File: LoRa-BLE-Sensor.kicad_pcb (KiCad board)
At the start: 4 copper layers, 96 x 80 mm, 123 parts, among them J1 SHF-105-01-X-D-SM, J2 Battery_Cell, J3 Conn_01x06_Socket, J4 Screw_Terminal_01x04, J5 Screw_Terminal_01x06, J6 Screw_Terminal_01x06, J7 Conn_01x10_Pin, J8 Conn_01x02_Socket, Q1 DMN67D7L, Q10 SQ2389ES, Q11 DMN62D0UDW-7, Q12 DMN62D0UDW-7, Q13 SQ2389ES, Q2 DMN67D7L, Q3 DMN67D7L, Q4 DMN67D7L, Q5 DMN67D7L, Q6 DMN67D7L, Q7 DMN67D7L, Q8 DMN67D7L, Q9 SQ2389ES, SW1 SW_Push, SW2 SW_Push, SW3 SW_Push, U1 RAK4630, U2 NPM1300-QEAA-R, U3 TLV61046ADBVR, U4 TLV61046ADBVR, U5 TLV61046ADBVR

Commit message: mounting holes + routing
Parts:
- added REF**: MountingHole_2.2mm_M2, MountingHole:MountingHole_2.2mm_M2, F.Cu at (67.5, 35.0)
- added REF**: MountingHole_2.2mm_M2, MountingHole:MountingHole_2.2mm_M2, F.Cu at (156.5, 35.0)
- added REF**: MountingHole_2.2mm_M2, MountingHole:MountingHole_2.2mm_M2, F.Cu at (67.5, 104.0)
- added REF**: MountingHole_2.2mm_M2, MountingHole:MountingHole_2.2mm_M2, F.Cu at (156.5, 104.0)
- moved D7 4.30 mm to (141.4, 59.8), turned to -90 degrees
- moved R8 0.55 mm to (130.3, 60.6)
- moved R11 0.06 mm to (127.8, 60.6)
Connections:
- Q3 pad 1: VOUT_SENSOR1 -> SENSOR1_PWR
- Q4 pad 1: VOUT_SENSOR1 -> SENSOR1_PWR
- Q7 pad 1: VOUT_SENSOR2 -> SENSOR2_PWR
- Q8 pad 1: VOUT_SENSOR2 -> SENSOR2_PWR
- R13 pad 1: VOUT_SENSOR2 -> SENSOR2_PWR
- R14 pad 1: VOUT_SENSOR2 -> SENSOR2_PWR
- R5 pad 1: VOUT_SENSOR1 -> SENSOR1_PWR
- R6 pad 1: VOUT_SENSOR1 -> SENSOR1_PWR
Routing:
- net VSYS: track 39.2 -> 140.7 mm, vias 11 -> 14
- net SENSOR2_IIN_NRF: track 2.31 -> 45.1 mm
- net SENSOR2_VIN_NRF: track 2.29 -> 41.5 mm
- net SENSOR2_PWR: track 33.7 -> 69.8 mm, vias 0 -> 4
- net SENSOR1_PWR: track 14.8 -> 50.2 mm, vias 0 -> 4
- net SENSOR3_D1_NRF: track 0.00 -> 34.4 mm
- net SENSOR3_D2_NRF: track 0.00 -> 33.3 mm
- net LDO2_OUT: track 45.2 -> 75.2 mm
- net VOUT_SENSOR1: track 24.9 -> 0.00 mm, vias 2 -> 0
- net BOOST2_FB_CTRL2: track 24.8 -> 43.9 mm
- net BOOST2_FB_CTRL1: track 25.7 -> 43.1 mm
- net VBOOST3: track 0.00 -> 17.0 mm
- net BOOST2_EN: track 27.3 -> 41.6 mm
- net SENSOR2_D1: track 1.70 -> 12.8 mm
- net SENSOR2_D2: track 1.70 -> 12.7 mm
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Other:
- board size 96 x 80 mm -> 96 x 79 mm

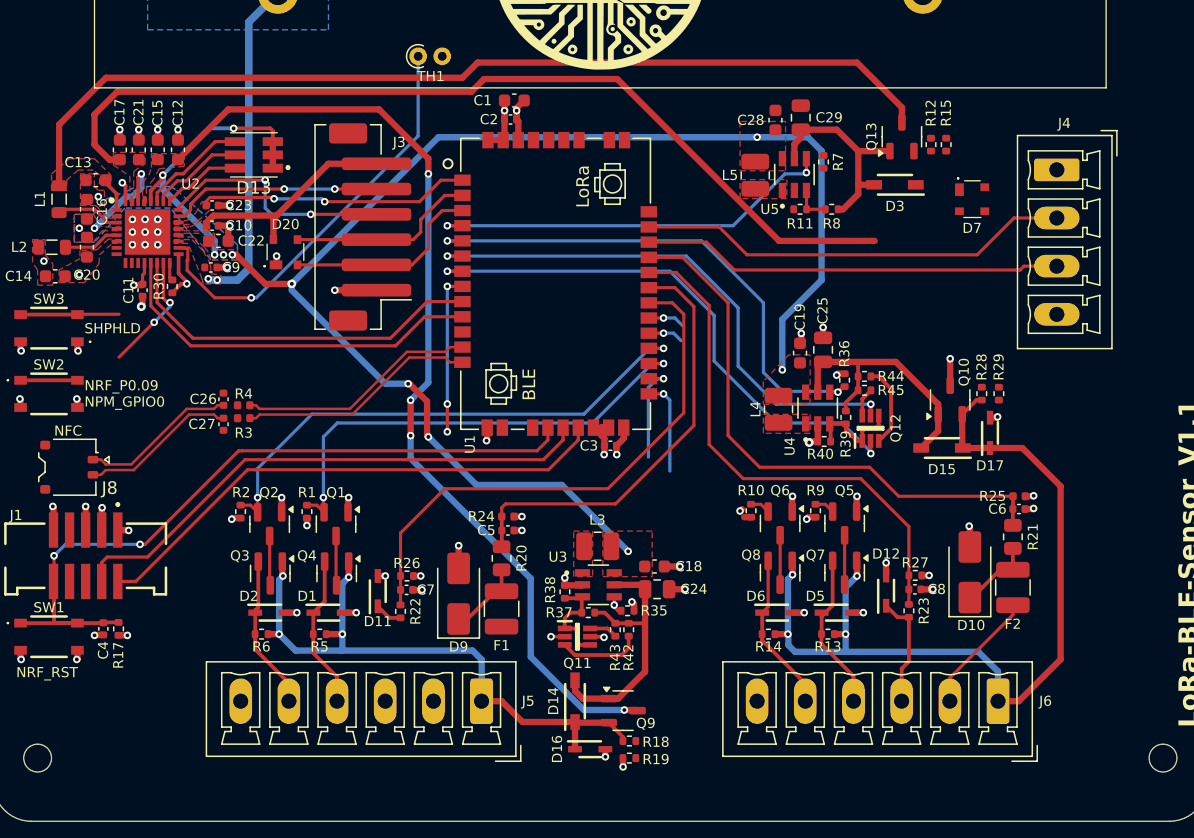
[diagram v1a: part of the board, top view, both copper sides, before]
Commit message: all tracks routed and DRC passed
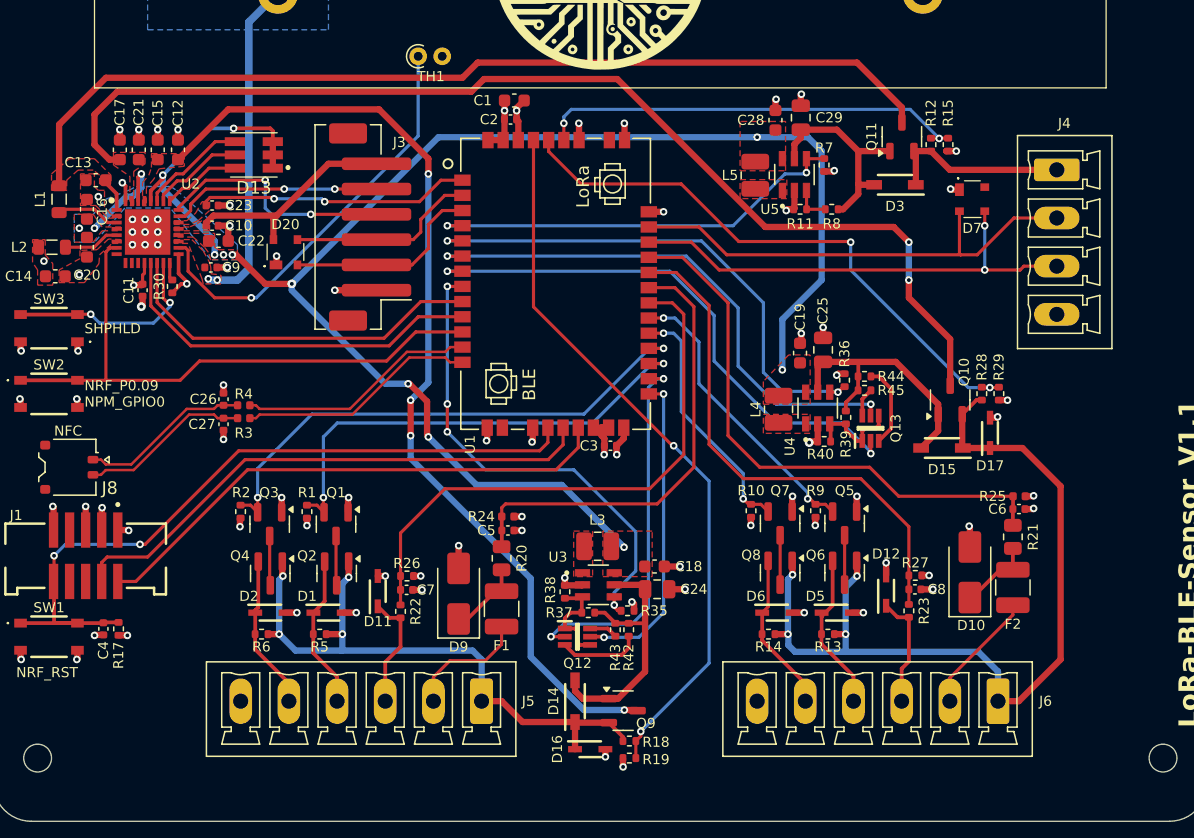
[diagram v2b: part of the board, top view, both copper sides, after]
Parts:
- moved R7 0.25 mm to (129.7, 57.1)
- moved R15 0.15 mm to (139.5, 55.5)
- renumbered Q13 to Q11, Q11 to Q12, Q12 to Q13, Q4 to Q2, Q2 to Q3, Q3 to Q4, Q7 to Q6, Q6 to Q7
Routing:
- net V_SENSOR1_READ: track 0.00 -> 57.1 mm, vias 0 -> 2
- net V_SENSOR2_READ: track 0.00 -> 46.2 mm, vias 0 -> 2
- net BUT1: track 4.50 -> 47.7 mm
- net V_SENSOR3_READ: track 0.00 -> 34.1 mm, vias 0 -> 2
- net BOOST1_EN: track 14.2 -> 38.8 mm
- net BOOST1_FB_CTRL2: track 9.25 -> 29.8 mm
- net SENSOR2_D1_NRF: track 4.64 -> 23.1 mm, vias 1 -> 2
- net BOOST1_FB_CTRL1: track 8.59 -> 25.1 mm
- net SENSOR2_D2_NRF: track 4.40 -> 19.7 mm, vias 1 -> 2
- net SENSOR3_PWR: track 0.00 -> 14.6 mm
- net LDO2_OUT: track 75.2 -> 88.5 mm, vias 1 -> 2
- net GND: track 59.6 -> 72.8 mm, vias 62 -> 75
- net SENSOR1_IIN: track 0.00 -> 9.77 mm
- net SENSOR1_VIN: track 2.18 -> 9.27 mm
- net SENSOR3_D2_NRF: track 33.3 -> 38.0 mm, vias 0 -> 2
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
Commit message: finished renaming and routing
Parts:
- removed the G*** at (43.2, 49.6)
- removed the J7 at (172.5, 75.5)
- added J8: Conn_01x04_Pin, Connector_PinHeader_2.54mm:PinHeader_1x04_P2.54mm_Vertical, F.Cu at (77.7, 98.3)
- added J9: Conn_01x04_Pin, Connector_PinHeader_2.54mm:PinHeader_1x04_P2.54mm_Vertical, F.Cu at (150.3, 84.8)
- renumbered C23 to C10, C16 to C11, C20 to C12, C22 to C13, C13 to C14, C14 to C15, C12 to C16, C15 to C17, C21 to C18, C17 to C19, C5 to C20, C6 to C21, C7 to C22, C8 to C23, C18 to C24, C24 to C25, C19 to C26, C25 to C27, C26 to C5, C27 to C6, C10 to C7, C9 to C8, C11 to C9, D13 to D1, D12 to D10, D14 to D11, D16 to D12, D15 to D13, D17 to D14, D3 to D15, D7 to D16, D20 to D2, D1 to D3, D2 to D4, D9 to D7, D10 to D8, D11 to D9, J8 to J2, J2 to J3, J3 to J4, J4 to J7, R4 to R1, R13 to R10, R10 to R11, R14 to R12, R20 to R13, R24 to R14, R21 to R15, R25 to R16, R22 to R17, R26 to R18, R23 to R19, R3 to R2, R27 to R20, R18 to R21, R19 to R22, R28 to R23, R29 to R24, R12 to R25, R15 to R26, R35 to R27, R37 to R28, R38 to R29, R17 to R3, R42 to R30, R43 to R31, R36 to R32, R39 to R33, R40 to R34, R44 to R35, R45 to R36, R7 to R37, R8 to R38, R11 to R39, R30 to R4, R1 to R5, R5 to R6, R2 to R7, R6 to R8
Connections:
- U2 pad 8: NPM_IO1 -> unconnected-(U2-GPIO1-Pad8)
- U2 pad 9: NPM_IO2 -> unconnected-(U2-GPIO2-Pad9)
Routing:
- net SENSOR2_D2_NRF: track 19.7 -> 49.4 mm
- net SENSOR1_D1_NRF: track 38.0 -> 65.8 mm
- net SENSOR2_D1_NRF: track 23.1 -> 46.6 mm
- net SENSOR1_D2_NRF: track 42.2 -> 63.5 mm
- net SENSOR2_PWR: track 69.8 -> 68.3 mm
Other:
- board text added: "D1_NRF"
- board text added: "S1"
- board text added: "S2"
- board text removed: "D6_NRF"
- board text removed: "D7_NRF"
- board text removed: "Vo1"
- board text removed: "Vo2"

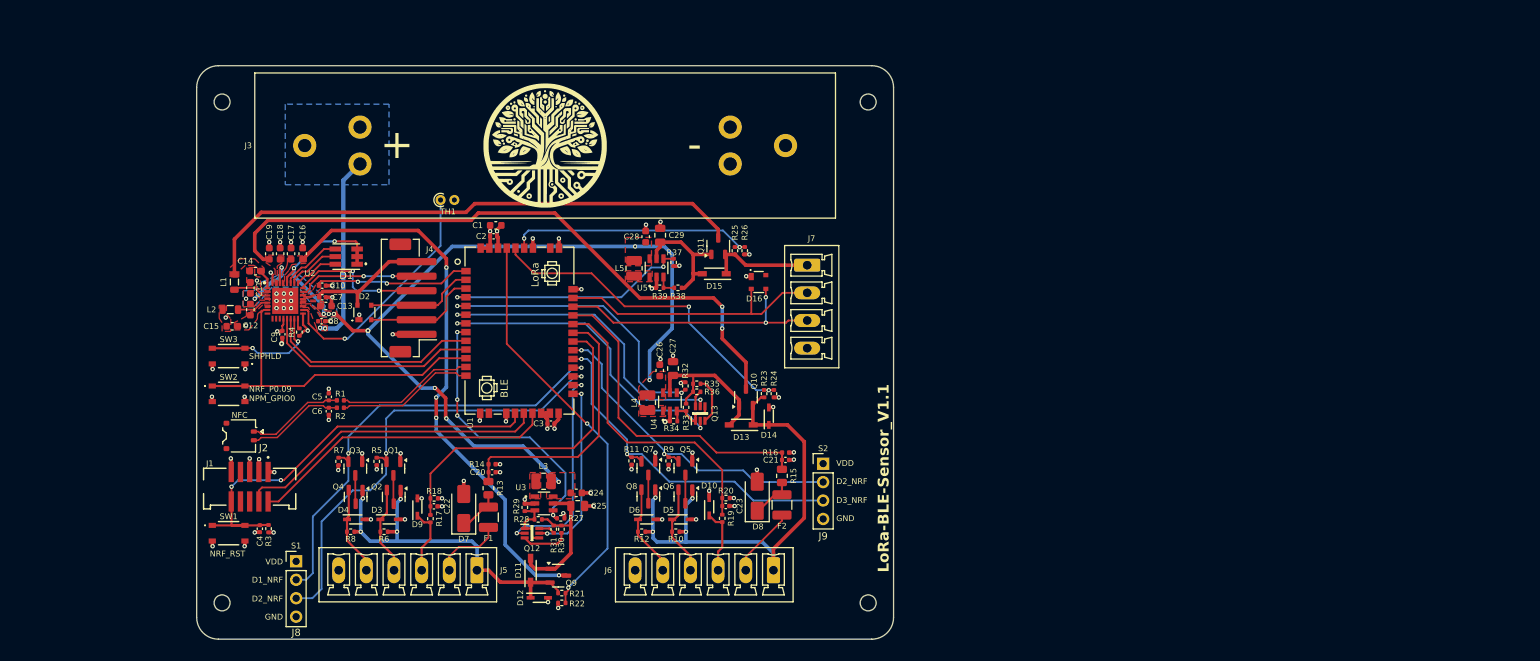
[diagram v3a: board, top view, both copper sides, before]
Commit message: replaced battery connectors
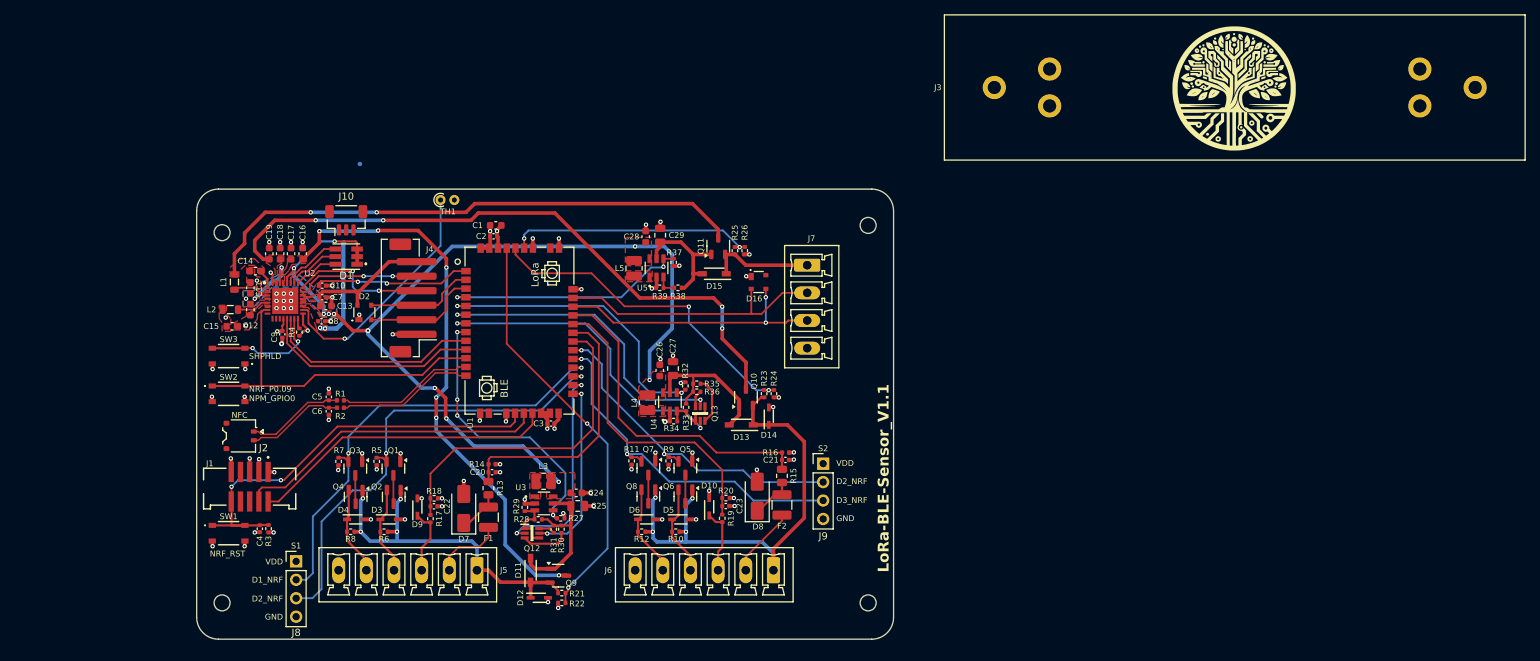
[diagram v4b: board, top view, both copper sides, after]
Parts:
- added J10: Battery_with_NTC, Connector_JST:JST_SH_BM03B-SRSS-TB_1x03-1MP_P1.00mm_Vertical, F.Cu at (84.6, 51.3)
- moved J3 95.3 mm to (207.0, 33.0)
- moved G*** 95.2 mm to (207.0, 33.0)
- moved REF** 18.0 mm to (67.5, 53.0)
- moved REF** 17.0 mm to (156.5, 52.0)
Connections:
- J3 pad 1: VBAT -> unconnected-(J3-+-Pad1)
- J3 pad 2: GND -> unconnected-(J3---Pad2)
- TH1 pad 1: Net-(U2-NTC) -> unconnected-(TH1-Pad1)
- TH1 pad 2: GND -> unconnected-(TH1-Pad2)
- U2 pad 18: Net-(U2-NTC) -> Net-(J10-NTC)
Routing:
- net Net-(U2-NTC): track 33.2 -> 0.00 mm, vias 1 -> 0
- net (no net): track 0.00 -> 33.2 mm, vias 0 -> 1
- net VBAT: track 26.4 -> 14.7 mm
- net LDO1_OUT: track 77.2 -> 78.1 mm, vias 4 -> 6
- net LDO2_OUT: track 88.5 -> 87.9 mm, vias 2 -> 4
- net V_BUCK1: track 78.7 -> 78.4 mm, vias 0 -> 2
- removed copper zone on B.Cu, net VBAT
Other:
- board size 96 x 79 mm -> 96 x 62 mm
- board text removed: "+"
- board text removed: "-"

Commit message: rearranged board down to 60mm
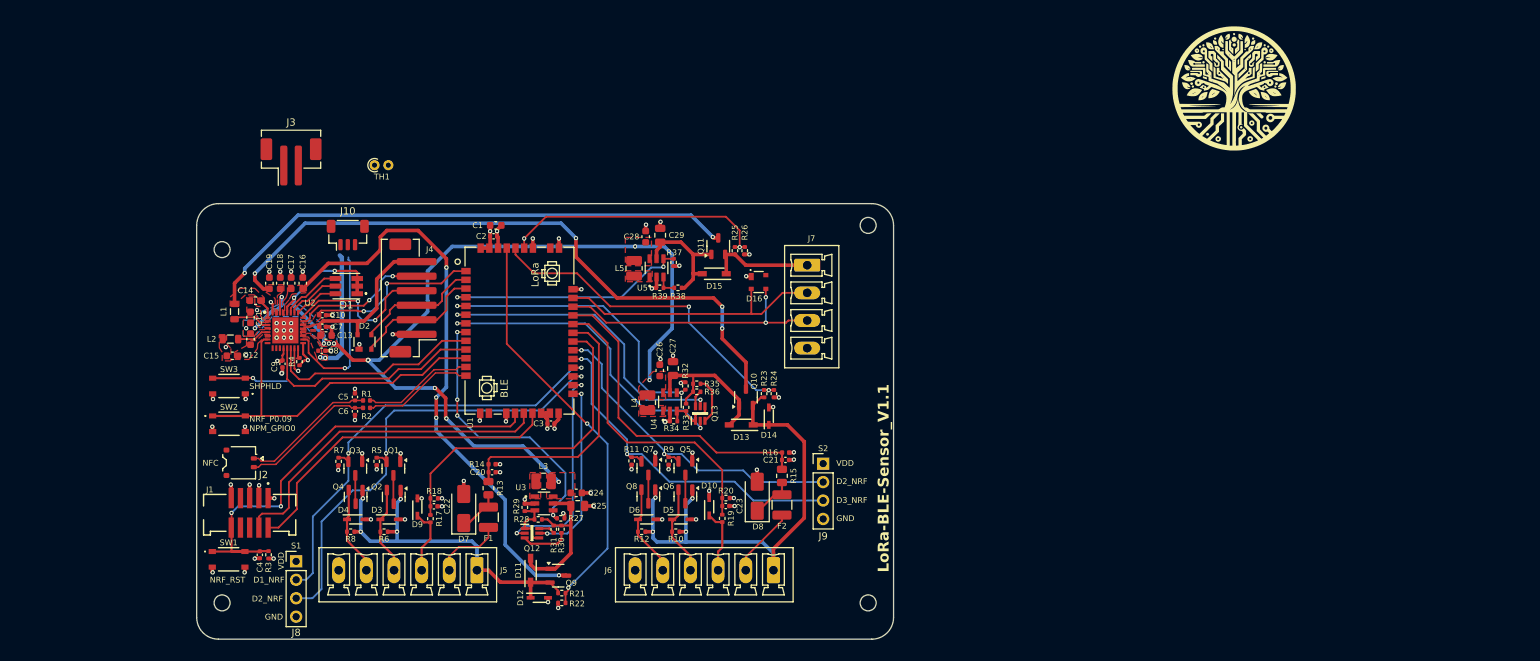
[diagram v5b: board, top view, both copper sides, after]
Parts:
- J3: footprint User_Connectors:18650_CLIP_PROTECTED -> Connector_JST:JST_PH_B2B-PH-SM4-TB_1x02-1MP_P2.00mm_Vertical
- moved J3 130.4 mm to (77.0, 43.2)
- moved TH1 10.3 mm to (88.5, 43.7)
- moved SW2 4.13 mm to (68.5, 79.3)
- moved SW3 4.13 mm to (68.5, 74.1)
- moved C11 4.07 mm to (71.4, 64.7)
- moved C12 4.07 mm to (71.4, 67.7)
- moved C13 4.07 mm to (81.8, 67.2)
- moved C14 4.07 mm to (72.1, 62.4)
- moved C16 4.07 mm to (78.6, 60.0)
- moved C17 4.07 mm to (77.0, 60.0)
- moved C18 4.07 mm to (75.5, 60.0)
- moved C19 4.07 mm to (74.0, 60.0)
- moved C7 4.07 mm to (81.3, 66.0)
- moved D1 4.07 mm to (84.6, 60.4)
- moved L1 4.07 mm to (69.2, 63.9)
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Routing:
- net (no net): track 33.2 -> 0.00 mm, vias 1 -> 0
- net Net-(J10-NTC): track 0.00 -> 24.2 mm, vias 0 -> 1
- net /NFC_OUT+: track 13.5 -> 18.7 mm
- net /NFC_OUT-: track 13.5 -> 18.7 mm
- net VBUS: track 17.6 -> 21.7 mm
- net SWDIO: track 42.4 -> 46.0 mm
- net NFC-: track 19.0 -> 15.4 mm
- net NFC+: track 19.0 -> 15.4 mm
- net SWCLK: track 43.2 -> 46.7 mm
- net RESET: track 58.9 -> 62.5 mm
- net VSYS: track 140.3 -> 143.3 mm
- net Net-(U2-SHPHLD): track 16.4 -> 13.7 mm
- net V_SENSOR3_READ: track 34.1 -> 36.7 mm
- net CC2: track 19.1 -> 21.7 mm
- net VBUS_NRF: track 21.6 -> 24.1 mm
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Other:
- board size 96 x 62 mm -> 96 x 60 mm

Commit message: external battery design finished
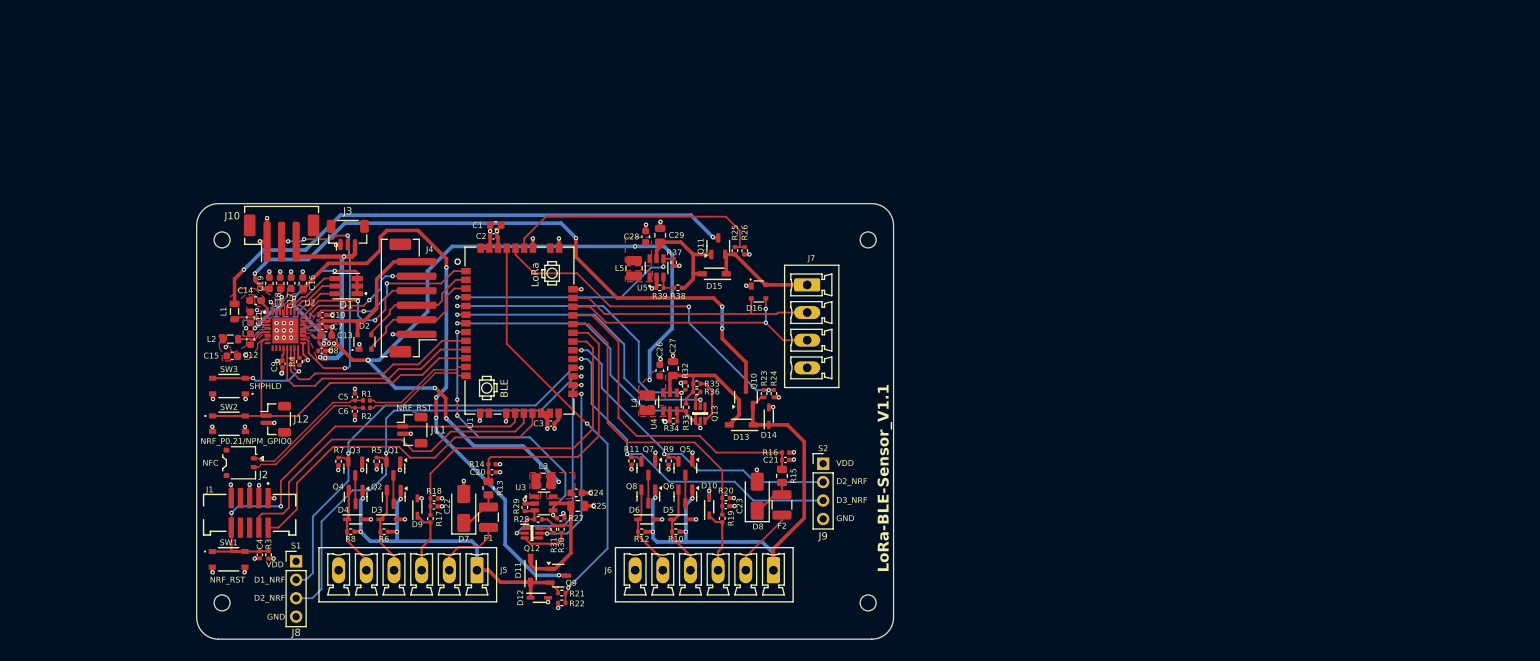
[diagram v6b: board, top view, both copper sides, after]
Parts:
- removed the J3 at (77.0, 43.2)
- removed TH1: 10K, Resistor_THT:R_Axial_DIN0204_L3.6mm_D1.6mm_P1.90mm_Vertical
- added J10: Battery_with_NTC, User_Connectors:JST_3PIN_PH_Vertical, F.Cu at (75.7, 53.8)
- added J11: Conn_01x02_Socket, User_Connectors:JST_SH_2-PIN_Vertical, F.Cu at (93.7, 80.2)
- added J12: Conn_01x02_Socket, User_Connectors:JST_SH_2-PIN_Vertical, F.Cu at (74.9, 78.7)
- G***: moved to B.Cu
- moved G*** 114.2 mm to (113.4, 98.5), turned to 180 degrees
- moved J7 2.72 mm to (148.1, 60.2)
- moved REF** 2.00 mm to (156.5, 54.0)
- moved REF** 1.34 mm to (67.5, 54.0)
- moved D16 1.30 mm to (141.4, 61.1)
- renumbered J10 to J3
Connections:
- net Net-(J10-NTC) renamed NTC
- net Net-(U2-SHPHLD) renamed /SHPHLD
- D16 pad 4: VOUT_SENSOR3 -> SENSOR3_PWR
- J3 pad 1: VBAT -> GND
- J3 pad 3: GND -> VBAT
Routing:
- net NTC: track 24.2 -> 38.0 mm, vias 1 -> 4
- net VBAT: track 16.9 -> 28.3 mm, vias 2 -> 3
- net GND: track 72.5 -> 79.7 mm, vias 75 -> 80
- net /SHPHLD: track 13.7 -> 16.2 mm
- net SENSOR3_D1_NRF: track 37.9 -> 35.4 mm
- net SWCLK: track 46.7 -> 48.1 mm
- net SWDIO: track 46.0 -> 47.2 mm
- net SENSOR3_PWR: track 14.6 -> 15.8 mm
- net SENSOR3_D2_NRF: track 38.0 -> 37.2 mm
- net V_SENSOR3_READ: vias 2 -> 0
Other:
- board text added: "NRF_P0.21/NPM_GPIO0"
- board text removed: "NRF_P0.09 NPM_GPIO0"
